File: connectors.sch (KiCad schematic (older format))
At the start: 15 parts, among them J1 2001-1-2-21-00-BK, P2 HOST, P3 CAM1, Q3 2N7002P.215

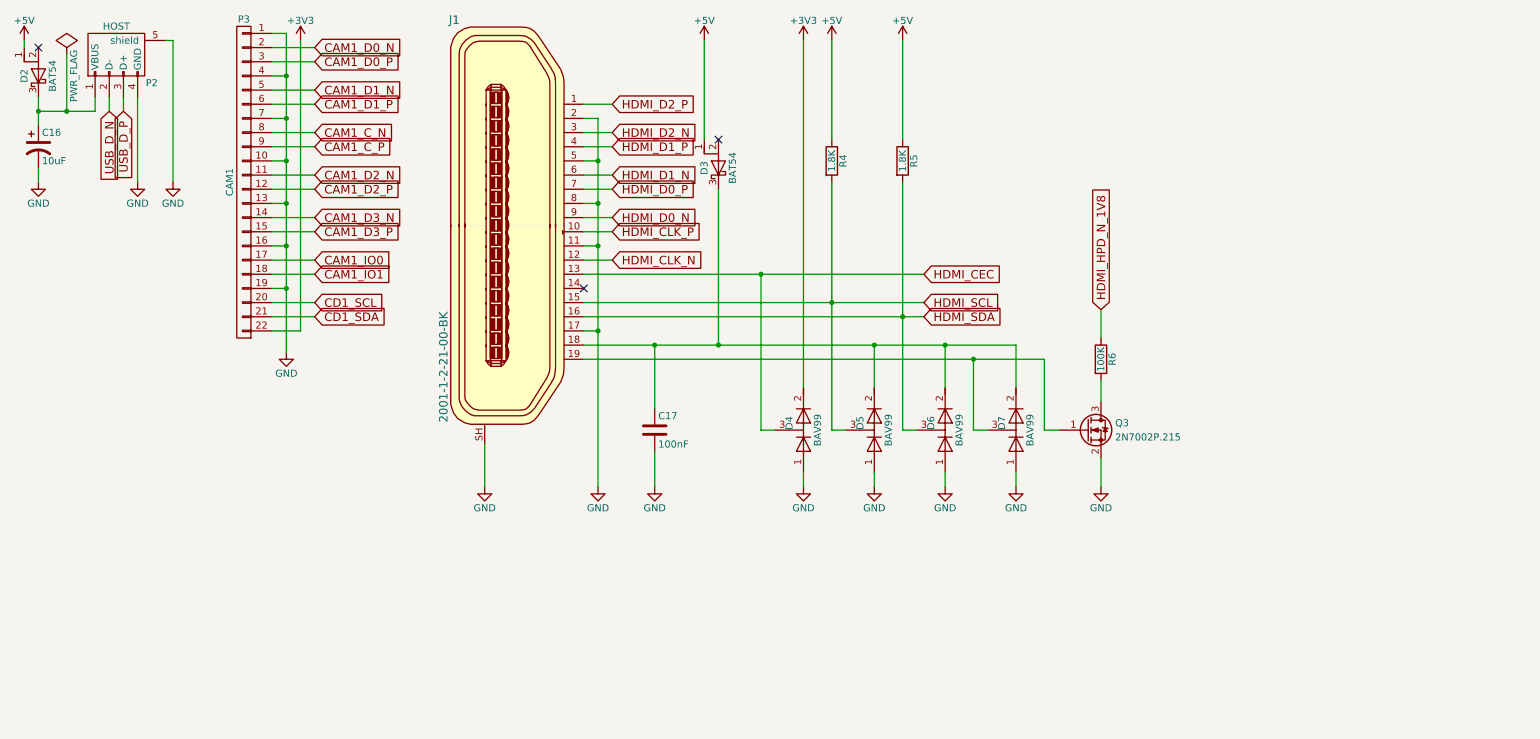
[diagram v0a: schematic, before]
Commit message: Partially routed gpio header
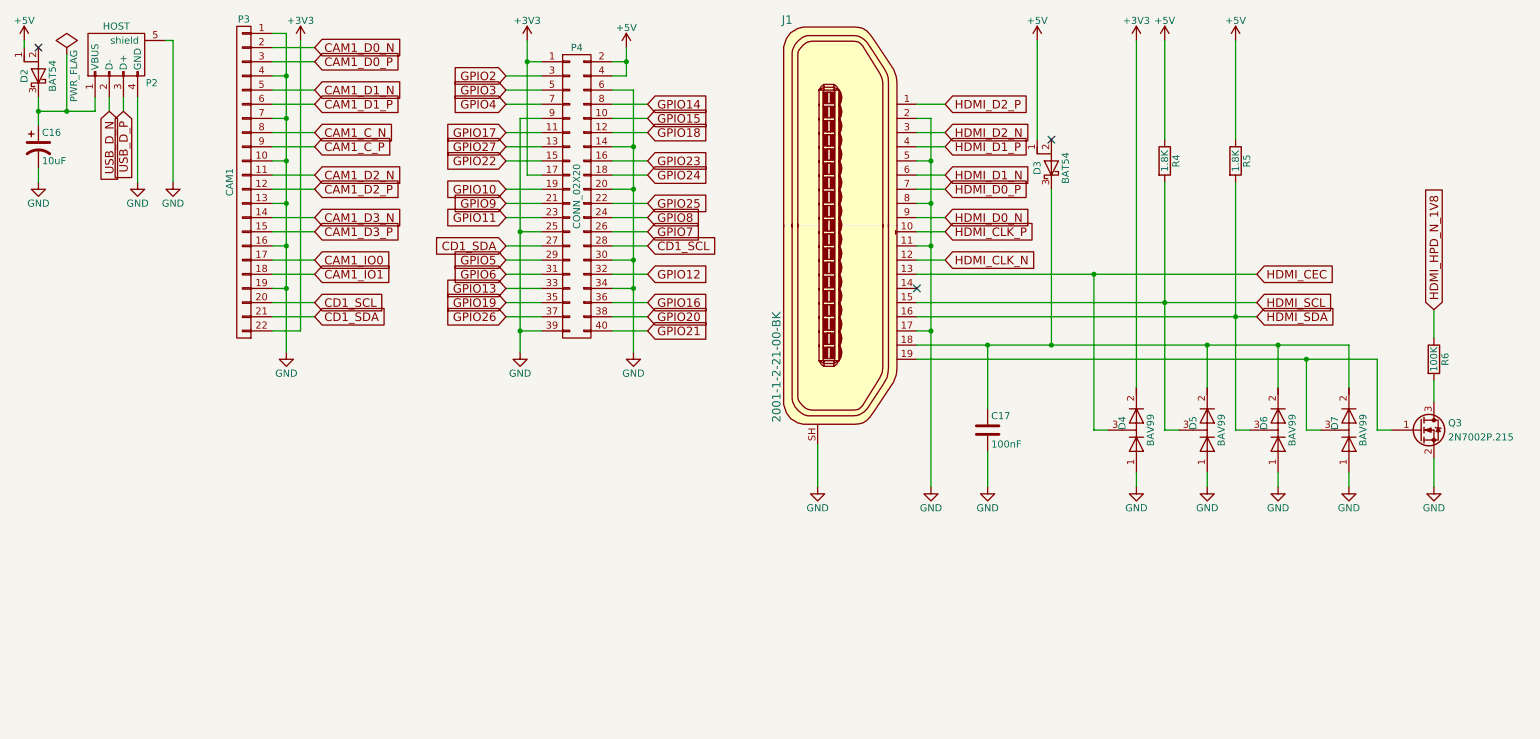
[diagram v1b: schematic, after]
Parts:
- added P4: CONN_02X20, Pin_Headers:Pin_Header_Straight_2x20, symbol CONN_02X20
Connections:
- net +3V3: now also P4.1 (P1), P4.17 (P17)
- net +5V: now also P4.2 (P2), P4.4 (P4)
- net CD1_SCL: now also P4.28 (P28)
- net CD1_SDA: now also P4.27 (P27)
- net GND: now also P4.14 (P14), P4.20 (P20), P4.25 (P25), P4.30 (P30), P4.34 (P34), P4.39 (P39), P4.6 (P6), P4.9 (P9)
- new net GPIO10: P4.19 (P19)
- new net GPIO11: P4.23 (P23)
- new net GPIO12: P4.32 (P32)
- new net GPIO13: P4.33 (P33)
- new net GPIO14: P4.8 (P8)
- new net GPIO15: P4.10 (P10)
- new net GPIO16: P4.36 (P36)
- new net GPIO17: P4.11 (P11)
- new net GPIO18: P4.12 (P12)
- new net GPIO19: P4.35 (P35)
- new net GPIO2: P4.3 (P3)
- new net GPIO20: P4.38 (P38)
- new net GPIO21: P4.40 (P40)
- new net GPIO22: P4.15 (P15)
- new net GPIO23: P4.16 (P16)
- new net GPIO24: P4.18 (P18)
- new net GPIO25: P4.22 (P22)
- new net GPIO26: P4.37 (P37)
- new net GPIO27: P4.13 (P13)
- new net GPIO3: P4.5 (P5)
- new net GPIO4: P4.7 (P7)
- new net GPIO5: P4.29 (P29)
- new net GPIO6: P4.31 (P31)
- new net GPIO7: P4.26 (P26)
- new net GPIO8: P4.24 (P24)
- new net GPIO9: P4.21 (P21)
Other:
- moved on the sheet: C17, D3, D4, D5, D6, D7, J1, Q3, R4, R5, R6

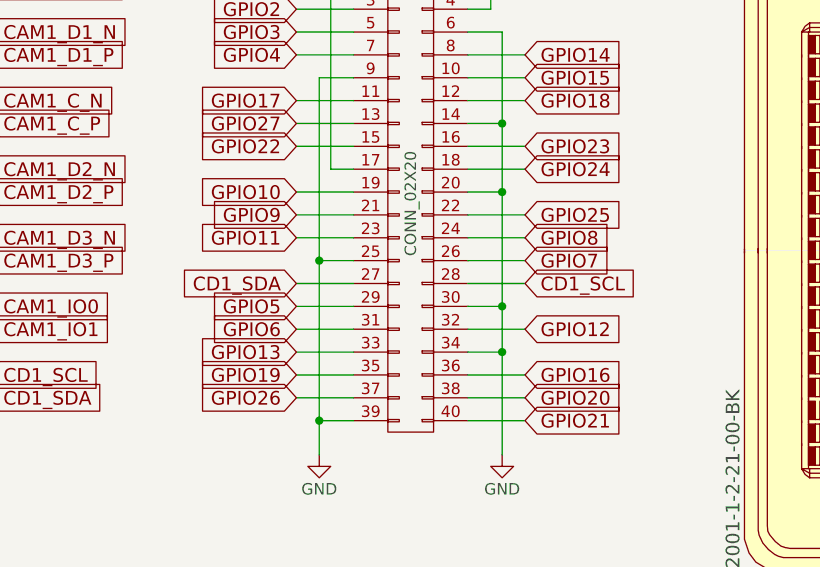
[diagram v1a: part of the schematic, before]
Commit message: Moved camera sda and scl to gpio 28 and 29
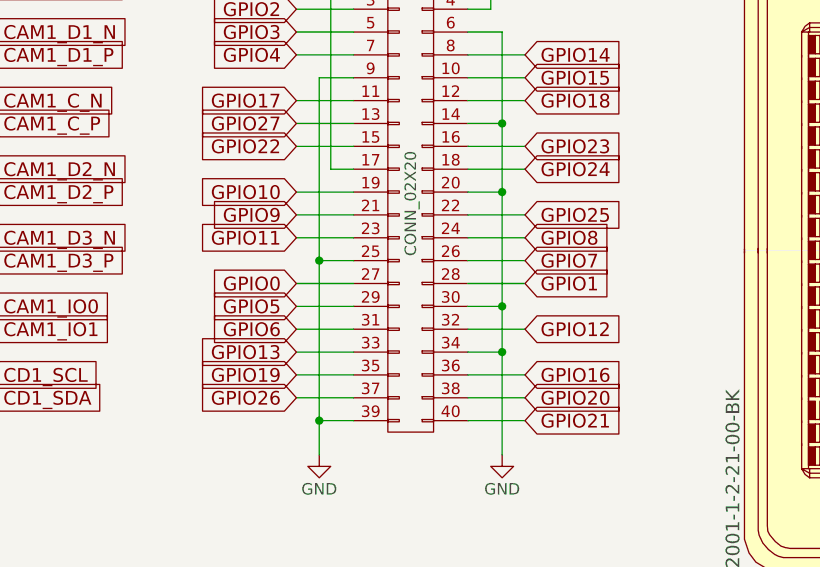
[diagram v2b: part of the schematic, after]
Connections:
- net CD1_SCL: no longer P4.28 (P28)
- net CD1_SDA: no longer P4.27 (P27)
- new net GPIO0: P4.27 (P27)
- new net GPIO1: P4.28 (P28)
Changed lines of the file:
@@
 	4700 2750 4950 2750
 Text GLabel 3950 2150 0    60   Input ~ 0
-CD1_SDA
+GPIO0
 Text GLabel 4950 2150 2    60   Input ~ 0
-CD1_SCL
+GPIO1
 Wire Wire Line
 	3950 2150 4200 2150

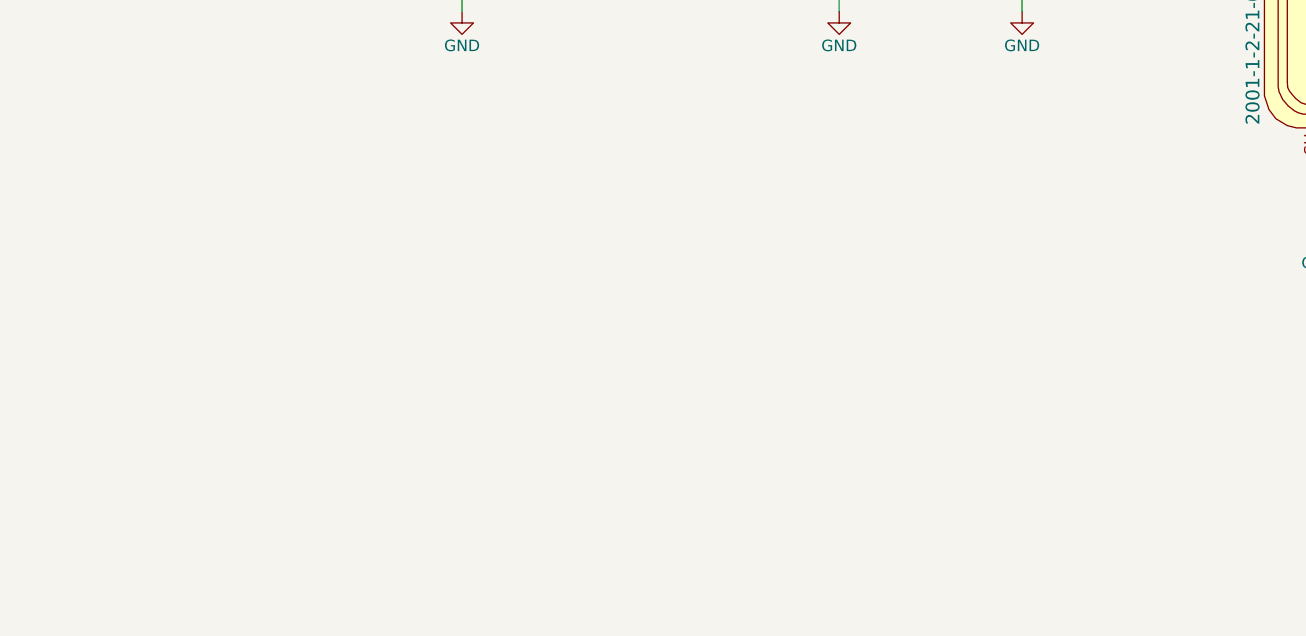
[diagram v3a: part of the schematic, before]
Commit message: Added audio jack
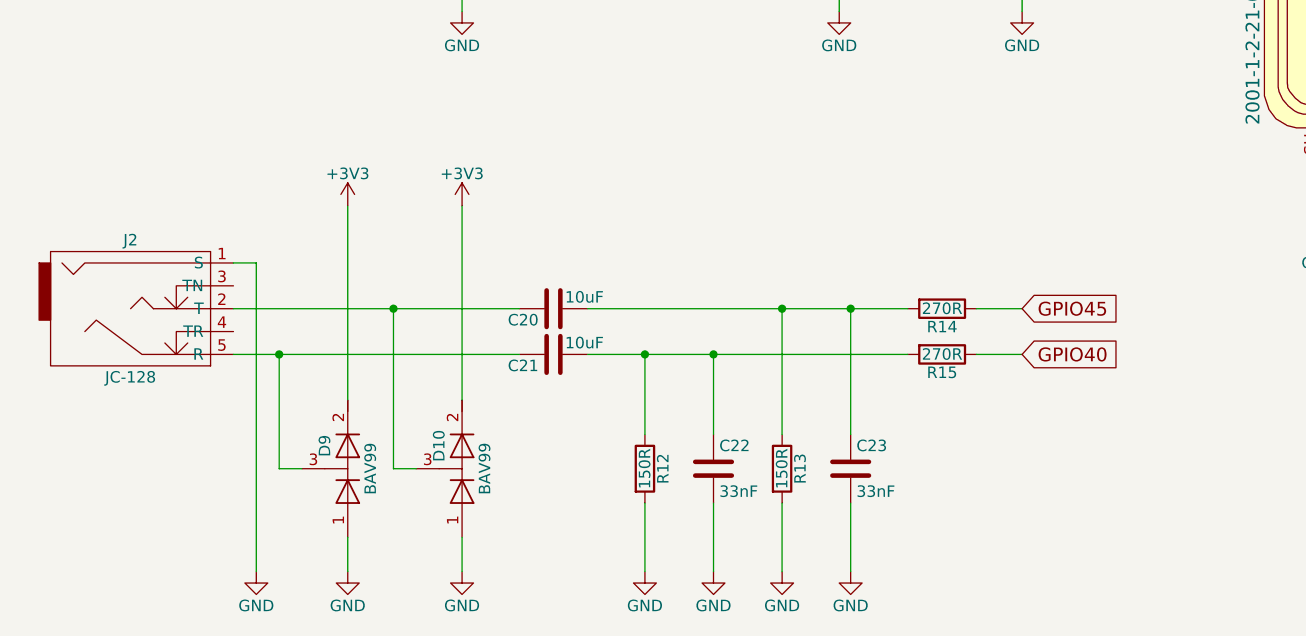
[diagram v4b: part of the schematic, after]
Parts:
- added C20, C21: 10uF, Capacitors_SMD:C_0805, symbol C
- added C22, C23: 33nF, Capacitors_SMD:C_0402, symbol C
- added D10, D9: BAV99, TO_SOT_Packages_SMD:SOT-23, symbol D_x2_Serial_AKC
- added J2: JC-128, jc-128:JC-128, symbol JACK_TRS_5PINS
- added R12, R13: 150R, Resistors_SMD:R_0603_HandSoldering, symbol R
- added R14, R15: 270R, Resistors_SMD:R_0603_HandSoldering, symbol R
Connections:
- net +3V3: now also D10.2 (K), D9.2 (K)
- net GND: now also C22.2, C23.2, D10.1 (A), D9.1 (A), J2.1 (S), R12.2, R13.2
- new net: C20.1, C23.1, R13.1, R14.2
- new net: C20.2, D10.3 (common), J2.2 (T)
- new net: C21.1, C22.1, R12.1, R15.2
- new net: C21.2, D9.3 (common), J2.5 (R)
- new net GPIO40: R15.1
- new net GPIO45: R14.1
